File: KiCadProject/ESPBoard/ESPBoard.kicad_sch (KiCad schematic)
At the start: 0 parts

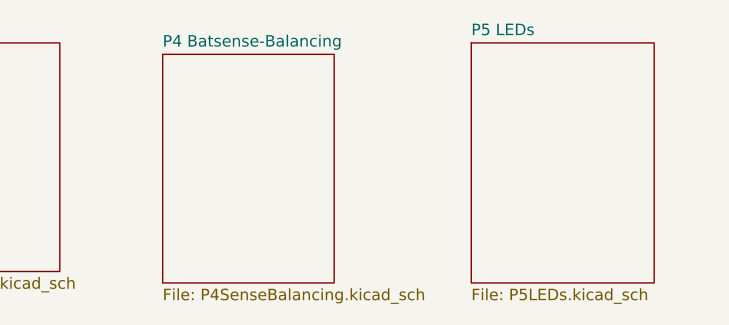
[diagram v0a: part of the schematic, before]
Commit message: ESP board layout mostly done. Small updates to battery management board
Signed-off-by: Eldalote.Electronics <Eldalote.Electronics@gmail.com>
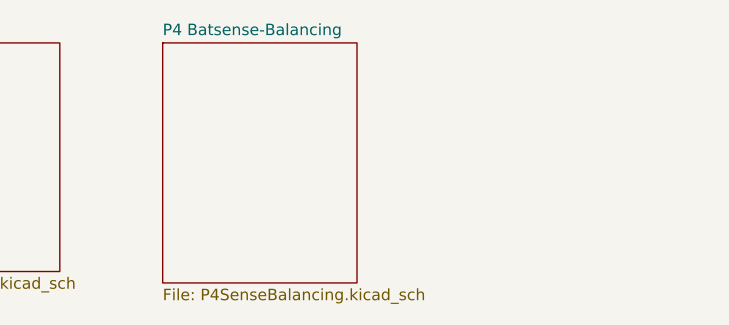
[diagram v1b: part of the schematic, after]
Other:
- removed sheet P5 LEDs

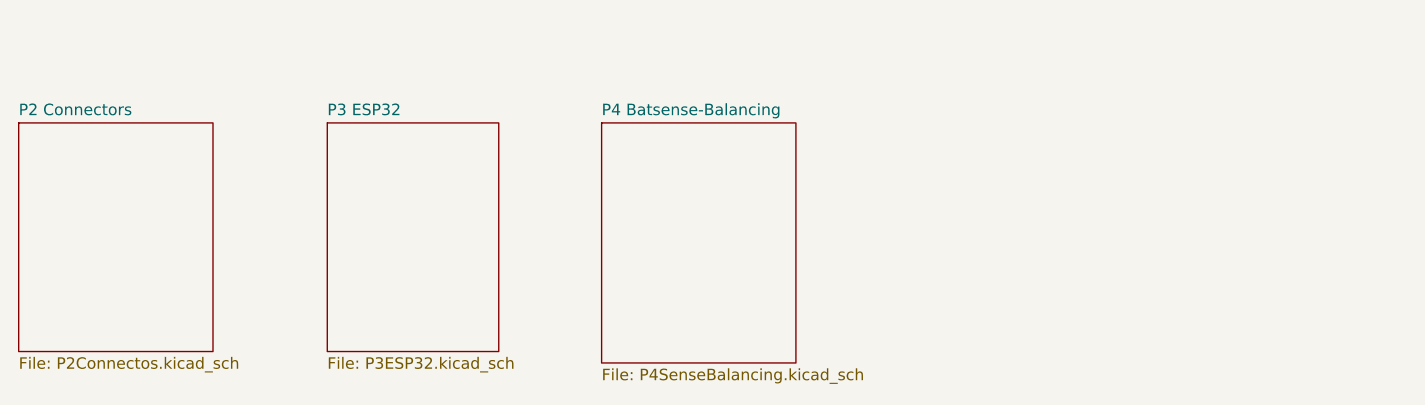
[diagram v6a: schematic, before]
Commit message: Made ready to order PCBs. Some problems with ordering due to misunderstanding. Thinking about solutions
Signed-off-by: Eldalote.Electronics <Eldalote.Electronics@gmail.com>
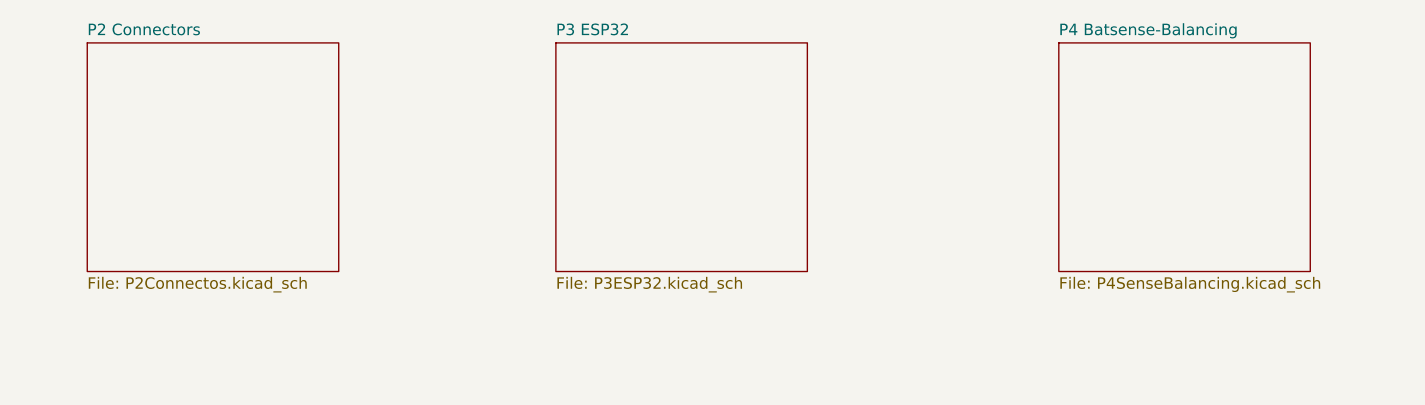
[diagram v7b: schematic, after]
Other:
- company: (none) -> Eldalote Electronics
- title: (none) -> ESP & Feedback Board
